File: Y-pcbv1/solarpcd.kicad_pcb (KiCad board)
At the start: 6 copper layers, 64 x 58 mm, 56 parts, among them IC2 TSL2561, J1 XF2M-1015-1A, J2 U.FL-R-SMT-1, J3 BATTERY CONNECTOR, U1 SWLP.12.B, U2 Value, U3 SW_SPDT, U4 SW_SPDT

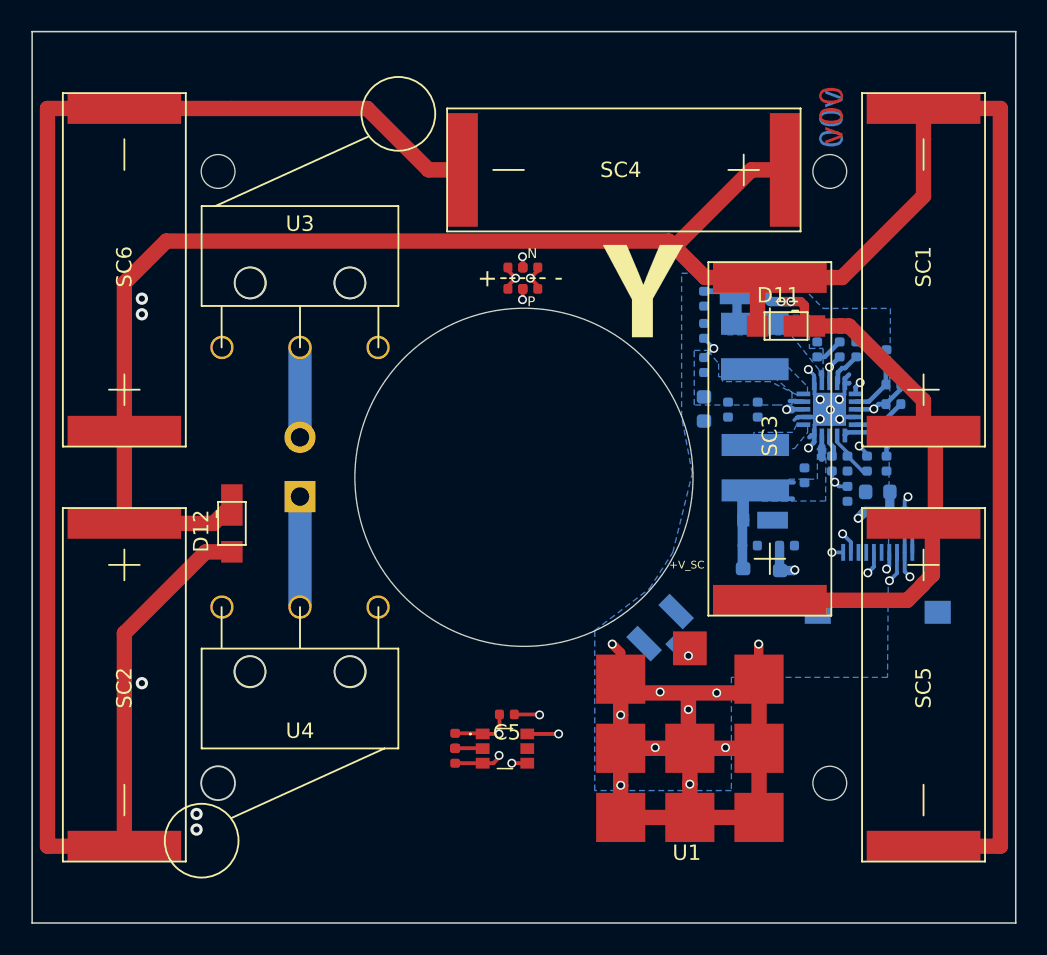
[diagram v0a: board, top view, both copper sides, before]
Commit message: Changed board outline to account for structures requirements
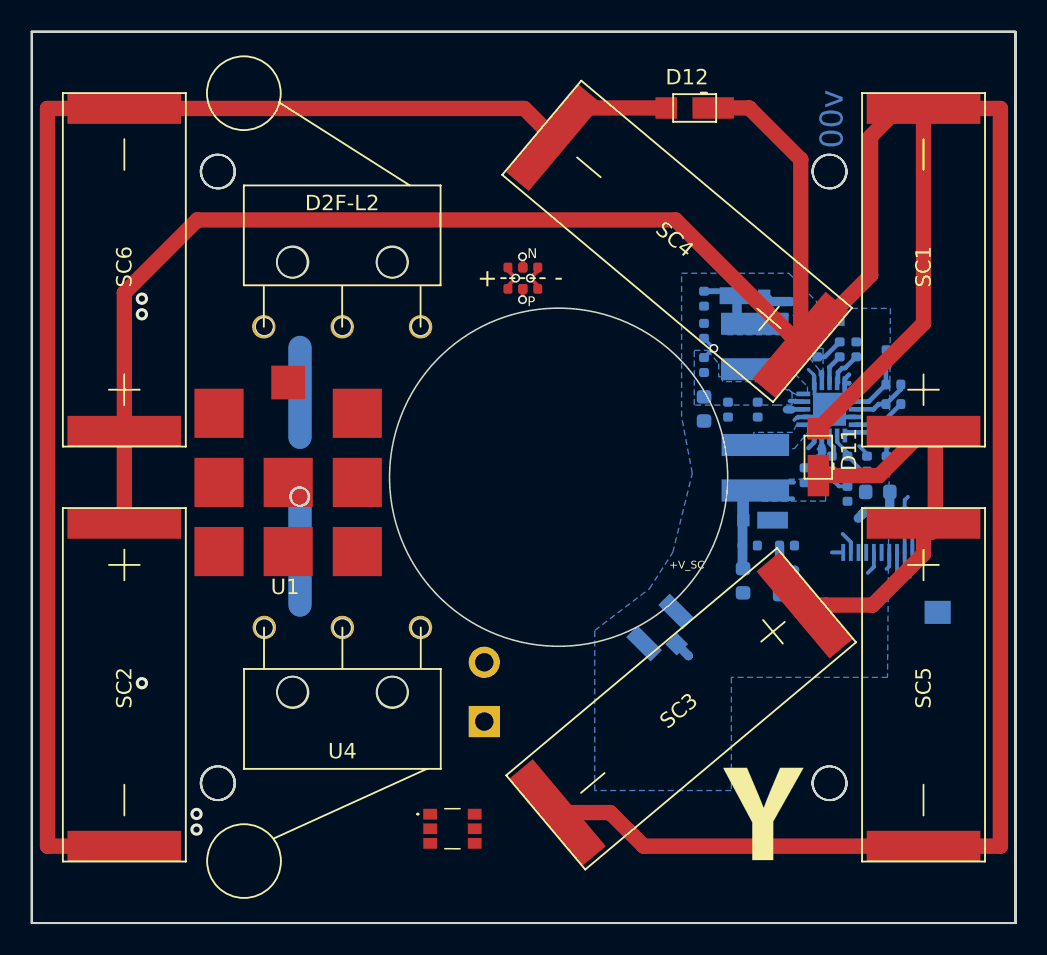
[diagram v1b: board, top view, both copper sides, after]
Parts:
- removed C5: 0.1uF, Capacitor_SMD:C_0402_1005Metric
- removed R10, R9: 0, Resistor_SMD:R_0402_1005Metric
- removed U3: SW_SPDT, custom-footprints:D2F-L2
- added D2F-L2: D2F-L2-2, solarpcb:D2F-L2-2, F.Cu at (133.2, 89.2)
- moved D12 40.5 mm to (156.1, 75.0), turned to 180 degrees
- moved Ref** 34.9 mm to (177.4, 119.9)
- moved U1 31.3 mm to (129.7, 99.3)
- moved J3 18.9 mm to (142.4, 114.7)
- moved SC4 11.4 mm to (163.0, 90.4), turned to 140 degrees
- moved D11 8.79 mm to (164.2, 97.7), turned to 90 degrees
- moved IC2 6.23 mm to (140.3, 121.9)
- moved U4 3.06 mm to (133.2, 108.8)
- moved SC3 2.29 mm to (163.3, 107.3), turned to 220 degrees
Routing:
- net GND: track 189.9 -> 116.8 mm, vias 19 -> 0
- net Net-(D11-Pad2): track 155.3 -> 209.6 mm
- net +3V3: track 46.0 -> 13.3 mm, vias 3 -> 0
- net Net-(J3-Pad1): track 7.11 -> 35.6 mm
- net Net-(D11-Pad1): track 38.1 -> 28.5 mm, vias 2 -> 0
- net SDA1: track 29.7 -> 27.7 mm, vias 2 -> 0
- net Net-(IC2-Pad2): track 1.80 -> 0.00 mm
- net SCL1: track 31.8 -> 30.8 mm, vias 2 -> 0
- net VOUT_EN: vias 2 -> 0
- net Net-(R2-Pad2): vias 2 -> 0
- net Net-(R11-Pad1): vias 2 -> 1
- net Net-(J2-Pad3): vias 1 -> 0
- net COIL_P: vias 2 -> 1
- net COIL_N: vias 2 -> 1
- net BATT_P: vias 1 -> 0
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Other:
- outline, holes or cut-outs redrawn

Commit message: Updated -Y PCB design
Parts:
- removed D2F-L2: D2F-L2-2, solarpcb:D2F-L2-2
- added U3: SW_SPDT, solarpcb:D2F-L2-2, F.Cu at (133.2, 89.2)
- D30: footprint custom-footprints:MICROSMP -> solarpcb:MICROSMP
- J1: footprint custom-footprints:XF2M-1015-1A -> solarpcb:XF2M-1015-1A
- U4: footprint custom-footprints:D2F-L2 -> solarpcb:D2F-L2
- moved J2 28.1 mm to (129.7, 94.5), turned to 0 degrees
- moved J1 27.7 mm to (152.5, 81.0), turned to 90 degrees
- moved C2 16.4 mm to (172.8, 90.8), turned to 0 degrees
- moved L1 14.5 mm to (174.2, 93.7)
- moved D30 13.0 mm to (171.0, 93.0), turned to 270 degrees
- moved D1 8.08 mm to (172.8, 89.8)
- moved C1 7.82 mm to (170.6, 106.5)
- moved C3 7.82 mm to (168.6, 97.1)
- moved C4 7.82 mm to (171.1, 97.1)
- moved C6 7.82 mm to (172.5, 106.3)
- moved D2 7.82 mm to (165.0, 108.2)
- moved L2 7.82 mm to (164.6, 104.8)
- moved R11 7.82 mm to (170.0, 97.1)
- moved R14 7.82 mm to (173.8, 107.6)
- moved R15 7.82 mm to (173.3, 108.8)
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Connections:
- IC2 pad 2: Net-(IC2-Pad2) -> (no net)
- IC2 pad 5: Net-(IC2-Pad5) -> (no net)
- J1 pad 5: BURN1 -> (no net)
- U4 pad 1: Net-(U4-Pad1) -> (no net)
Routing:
- net GND: track 116.8 -> 152.7 mm, vias 0 -> 1
- net +3V3: track 13.3 -> 46.9 mm
- net SCL1: track 30.8 -> 0.00 mm
- net BATT_P: track 55.7 -> 26.1 mm
- net SDA1: track 27.7 -> 0.00 mm
- net Net-(J3-Pad1): track 35.6 -> 12.7 mm
- net Net-(J3-Pad2): track 5.85 -> 26.4 mm
- net /VBAT: track 14.1 -> 2.40 mm
- net Net-(L1-Pad2): track 0.00 -> 10.8 mm
- net Net-(R11-Pad1): track 11.8 -> 3.79 mm
- net VOUT_EN: track 9.76 -> 1.74 mm
- net BATT_N: track 55.6 -> 49.4 mm
- net VSOLAR: track 6.82 -> 11.3 mm
- net Net-(R2-Pad2): track 7.46 -> 3.93 mm
- net COIL_N: track 31.4 -> 29.3 mm
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- removed copper zone on B.Cu, net +3V3
- removed copper zone on B.Cu, net GND
- removed copper zone on In3.Cu, net GND
- removed copper zone on B.Cu, net Net-(C11-Pad1)
- removed copper zone on B.Cu, net Net-(L1-Pad2)
- removed copper zone on B.Cu, net VSOLAR
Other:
- outline, holes or cut-outs redrawn
- board text removed: "+BATT"
- board text removed: "+V_SC"
- board text removed: "-BATT"

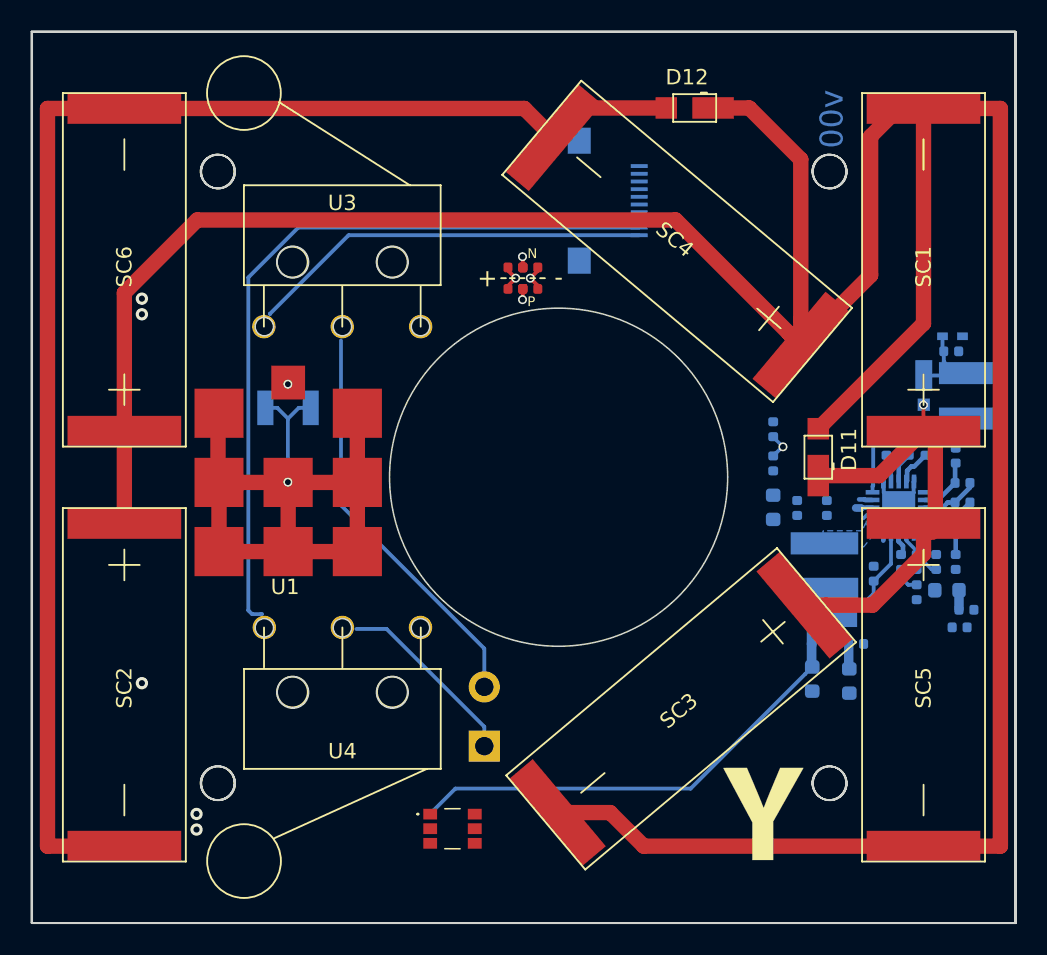
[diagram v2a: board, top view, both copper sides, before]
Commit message: Updated -Y PCB Layout
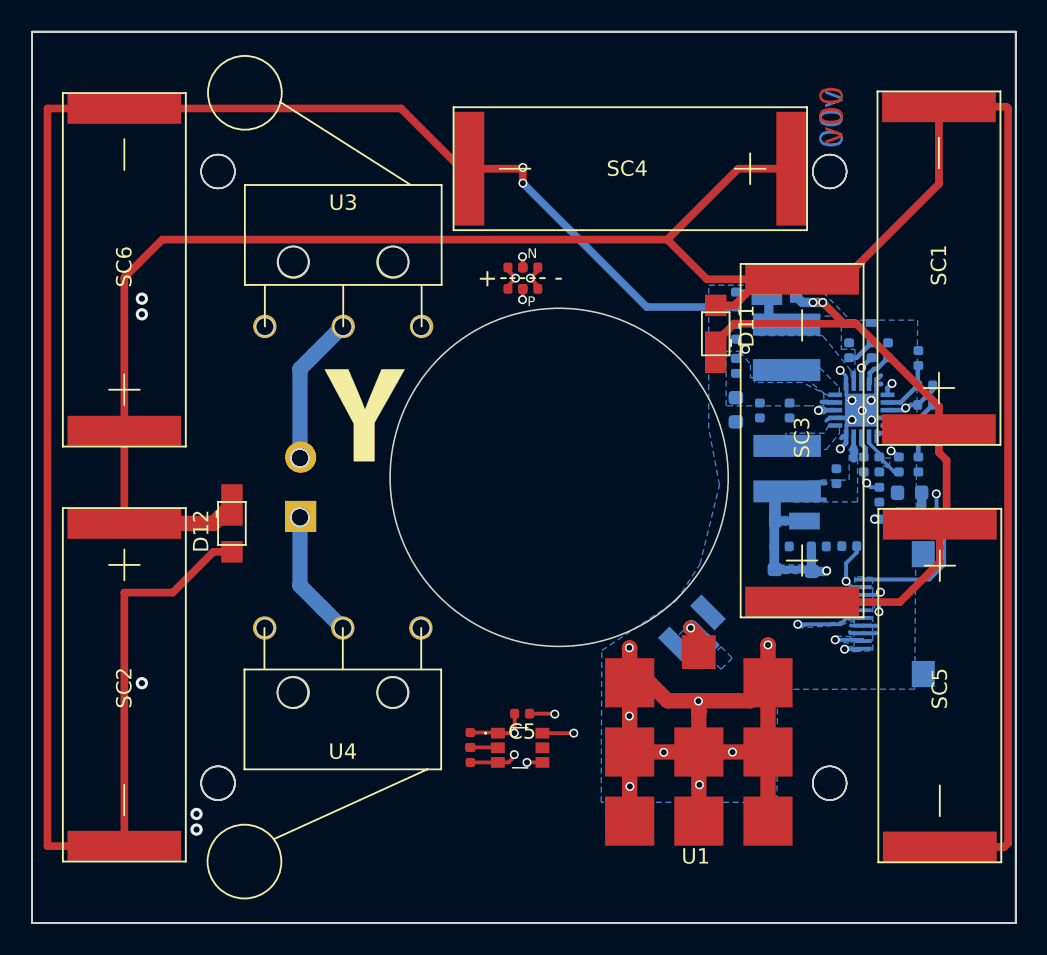
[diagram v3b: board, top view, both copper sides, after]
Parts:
- added C5: 0.1uF, Capacitor_SMD:C_0402_1005Metric, F.Cu at (144.9, 114.4)
- added R10: 0, Resistor_SMD:R_0402_1005Metric, F.Cu at (141.5, 117.1)
- added R9: 0, Resistor_SMD:R_0402_1005Metric, F.Cu at (141.5, 116.1)
- D30: footprint solarpcb:MICROSMP -> custom-footprints:MICROSMP
- U4: footprint solarpcb:D2F-L2 -> custom-footprints:D2F-L2
- moved D12 40.5 mm to (126.0, 102.0), turned to 270 degrees
- moved Ref** 36.7 mm to (151.5, 94.0)
- moved U1 32.0 mm to (156.4, 116.9)
- moved J1 30.6 mm to (167.1, 107.9), turned to 270 degrees
- moved J2 29.9 mm to (155.9, 108.8), turned to 225 degrees
- moved J3 19.1 mm to (130.5, 101.4)
- moved C2 14.4 mm to (158.8, 87.4), turned to 270 degrees
- moved L1 12.5 mm to (162.1, 90.5)
- moved SC4 11.5 mm to (162.4, 78.9), turned to 180 degrees
- moved D30 11.2 mm to (161.5, 87.2), turned to 0 degrees
- moved D11 10.4 mm to (157.5, 89.7)
- moved R15 8.91 mm to (166.2, 103.5)
- moved IC2 6.87 mm to (144.8, 116.6)
- moved C1 6.79 mm to (168.1, 100.1)
- moved C12 6.79 mm to (161.3, 105.8)
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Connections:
- IC2 pad 2: (no net) -> Net-(IC2-Pad2)
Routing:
- net /coil: track 16503.7 -> 15901.0 mm
- net GND: track 152.7 -> 207.7 mm, vias 1 -> 19
- net Net-(D11-Pad2): track 209.6 -> 165.4 mm
- net BATT_P: track 26.1 -> 68.6 mm, vias 0 -> 1
- net COIL_N: track 29.3 -> 71.4 mm, vias 1 -> 2
- net COIL_P: track 28.8 -> 67.6 mm, vias 1 -> 2
- net SCL1: track 0.00 -> 29.5 mm, vias 0 -> 2
- net SDA1: track 0.00 -> 27.0 mm, vias 0 -> 2
- net Net-(J3-Pad2): track 26.4 -> 9.79 mm
- net Net-(D11-Pad1): track 28.3 -> 44.6 mm, vias 1 -> 2
- net /VBAT: track 2.40 -> 14.2 mm, vias 0 -> 2
- net Net-(L1-Pad2): track 10.8 -> 0.00 mm
- net Net-(R11-Pad1): track 3.79 -> 12.0 mm, vias 1 -> 2
- net VOUT_EN: track 1.74 -> 9.76 mm, vias 0 -> 2
- net +3V3: track 46.9 -> 53.7 mm, vias 0 -> 3
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- added copper zone on B.Cu, net +3V3
- added copper zone on B.Cu, net GND
- added copper zone on In3.Cu, net GND
- added copper zone on B.Cu, net Net-(C11-Pad1)
- added copper zone on B.Cu, net Net-(L1-Pad2)
- added copper zone on B.Cu, net VSOLAR
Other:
- outline, holes or cut-outs redrawn
- rule pad_to_mask_clearance: 0.0508 -> 0
- board text added: "+BATT"
- board text added: "-BATT"

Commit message: Modified -Y Layout
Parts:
- moved J1 20.6 mm to (163.1, 87.7)
- moved C13 10.2 mm to (160.4, 115.5)
- moved D2 10.2 mm to (159.2, 111.5)
- moved R15 10.2 mm to (162.8, 113.1)
- moved C12 10.2 mm to (158.0, 115.4)
- moved C14 10.2 mm to (160.8, 113.1)
- moved C10 10.2 mm to (158.4, 113.1)
- moved L2 9.98 mm to (159.5, 108.0)
- moved C3 6.01 mm to (162.2, 95.3)
- moved C4 6.01 mm to (164.7, 95.3)
- moved D1 6.01 mm to (162.9, 93.5)
- moved J2 6.01 mm to (152.0, 113.4)
- moved R11 6.01 mm to (163.7, 95.3)
- moved R14 6.01 mm to (167.4, 105.8)
- moved R3 6.01 mm to (166.7, 95.8)
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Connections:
- C10 pad 1: +3V3 -> GND
- C12 pad 1: +3V3 -> GND
- C13 pad 1: +3V3 -> GND
- C14 pad 1: +3V3 -> GND
- D2 pad 1: +3V3 -> GND
- D2 pad 2: +3V3 -> GND
- L2 pad 2: +3V3 -> GND
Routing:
- net BATT_N: track 46.6 -> 100.8 mm
- net COIL_N: track 71.4 -> 23.4 mm
- net COIL_P: track 67.6 -> 22.6 mm
- net SCL1: track 29.5 -> 49.6 mm
- net SDA1: track 27.0 -> 45.6 mm
- net Net-(C11-Pad1): track 0.89 -> 17.1 mm
- net VSOLAR: track 6.82 -> 18.7 mm
- net Net-(L1-Pad2): track 0.00 -> 10.9 mm
- net Net-(R11-Pad1): track 12.0 -> 22.1 mm
- net GND: track 207.7 -> 199.1 mm, vias 19 -> 17
- net +3V3: track 53.7 -> 45.3 mm
- net Net-(J2-Pad3): track 3.40 -> 11.0 mm
- net Net-(D11-Pad1): track 44.6 -> 46.0 mm
- net BATT_P: track 68.6 -> 67.7 mm
- removed copper zone on B.Cu, net Net-(C11-Pad1)
- removed copper zone on B.Cu, net Net-(L1-Pad2)
- removed copper zone on B.Cu, net VSOLAR

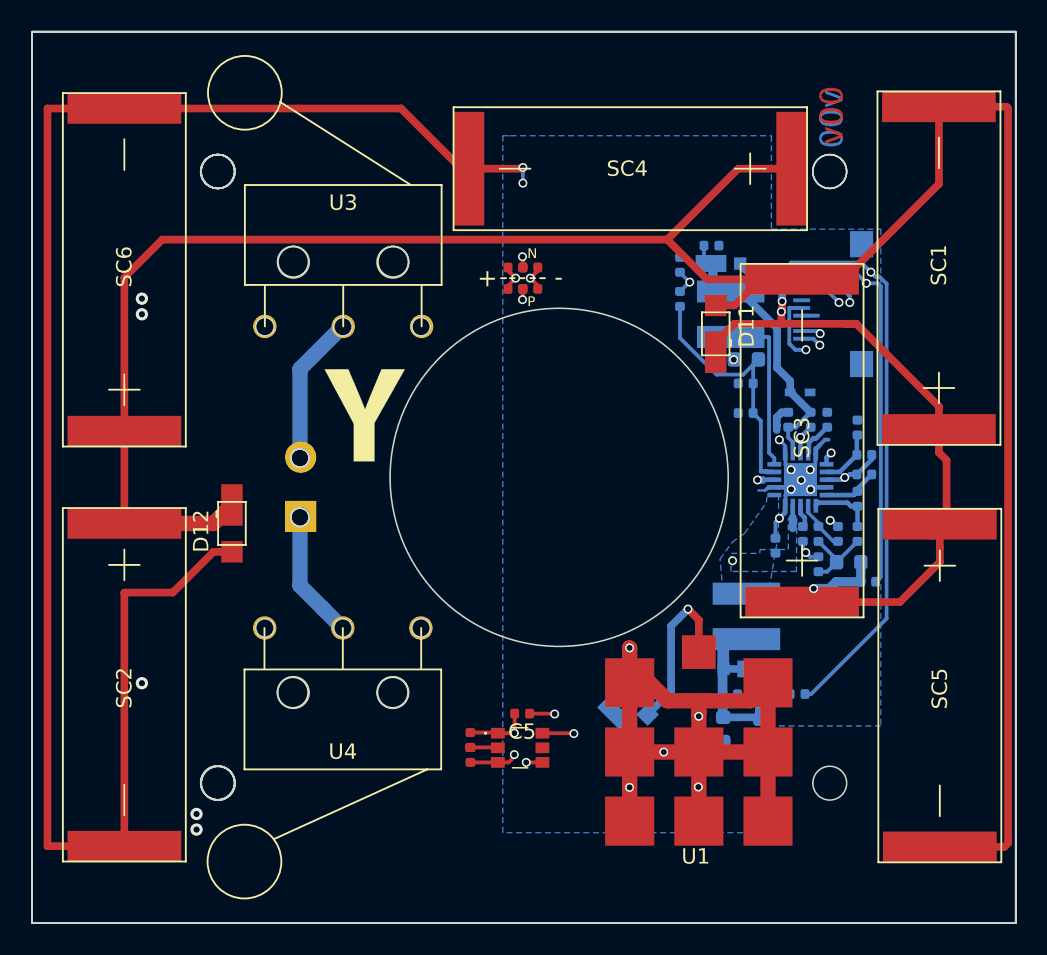
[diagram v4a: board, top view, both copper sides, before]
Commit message: Updated -Y PCB Layout
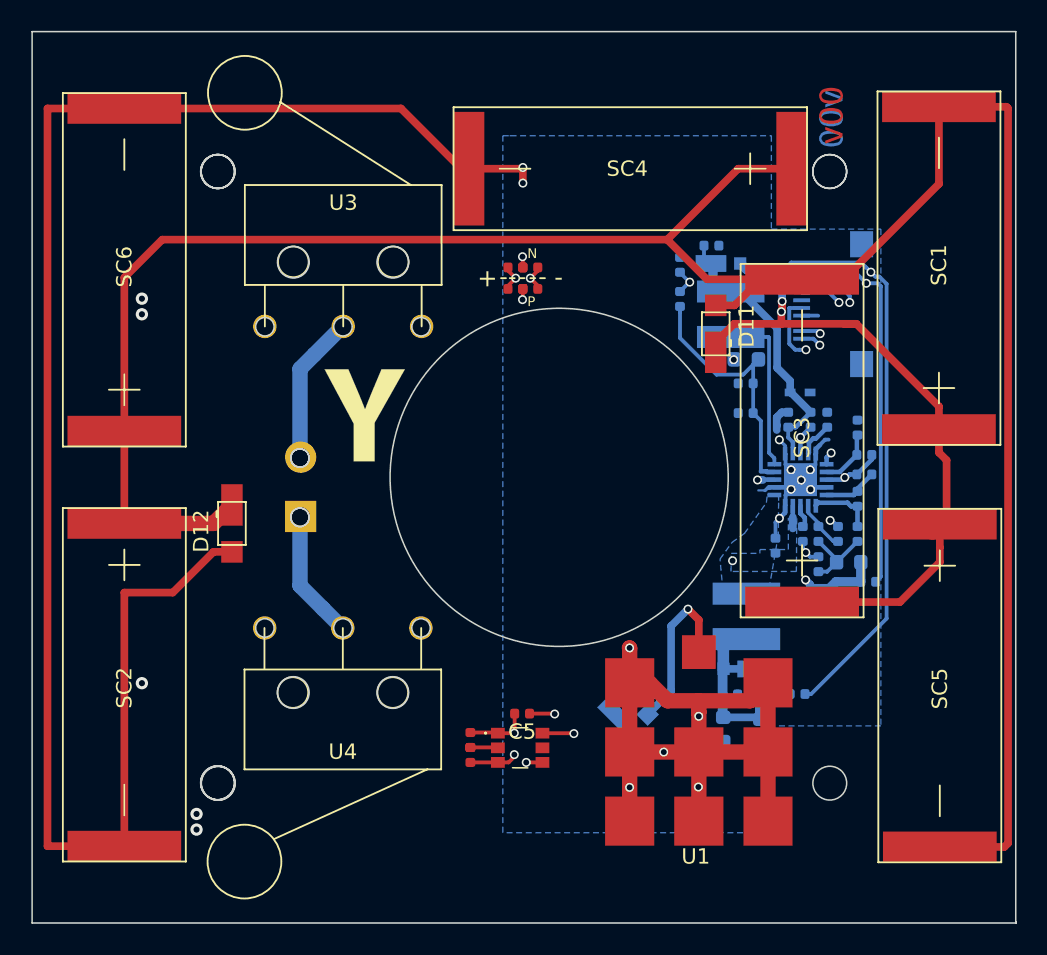
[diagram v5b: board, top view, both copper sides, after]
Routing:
- net /VBAT: track 14.2 -> 14.8 mm
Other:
- outline, holes or cut-outs redrawn
